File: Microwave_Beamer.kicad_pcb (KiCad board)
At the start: 4 copper layers, 200 x 170 mm, 409 parts, among them IC1 MAX2870ETJ+, U1 SKY13575-639LF, U10 SKY13575-639LF, U11 SKY13575-639LF, U12 SKY13575-639LF, U13 SE5023L-R, U14 SE5023L-R, U15 SE5023L-R, U16 SE5023L-R, U17 SE5023L-R, U18 SE5023L-R, U19 SE5023L-R, U2 SKY13575-639LF, U20 SE5023L-R, U21 SE5023L-R, U22 SE5023L-R, U23 SE5023L-R, U24 SE5023L-R, U25 SE5023L-R, U26 SE5023L-R, U27 SE5023L-R, U28 SE5023L-R, U29 SE5023L-R, U3 SKY13575-639LF, U30 SE5023L-R, U31 SE5023L-R, U32 SE5023L-R, U33 SE5023L-R, U34 SE5023L-R, U35 SE5023L-R, U36 SE5023L-R, U37 SE5023L-R, U38 SE5023L-R, U39 SE5023L-R, U4 SKY13575-639LF, U40 SE5023L-R, U41 SE5023L-R, U42 SE5023L-R, U43 SE5023L-R, U44 SE5023L-R, U45 SE5023L-R, U46 SE5023L-R, U47 SE5023L-R, U48 SE5023L-R, U49 SE5023L-R, U5 SKY13575-639LF, U50 LDL1117S33R, U51 SN74LVC1G14DCKR, U52 MIC5219-2.85YM5-TR, U53 SN74LVC1G14DCKR, U54 74HC138D, U55 TPS548D26RXXR, U56 PI_PICO, U57 SN74LVC1G14DCKR, U6 SKY13575-639LF, U7 SKY13575-639LF, U8 SKY13575-639LF, U9 SKY13575-639LF, Y1 ECS-3225MVQ-1000-CN-TR

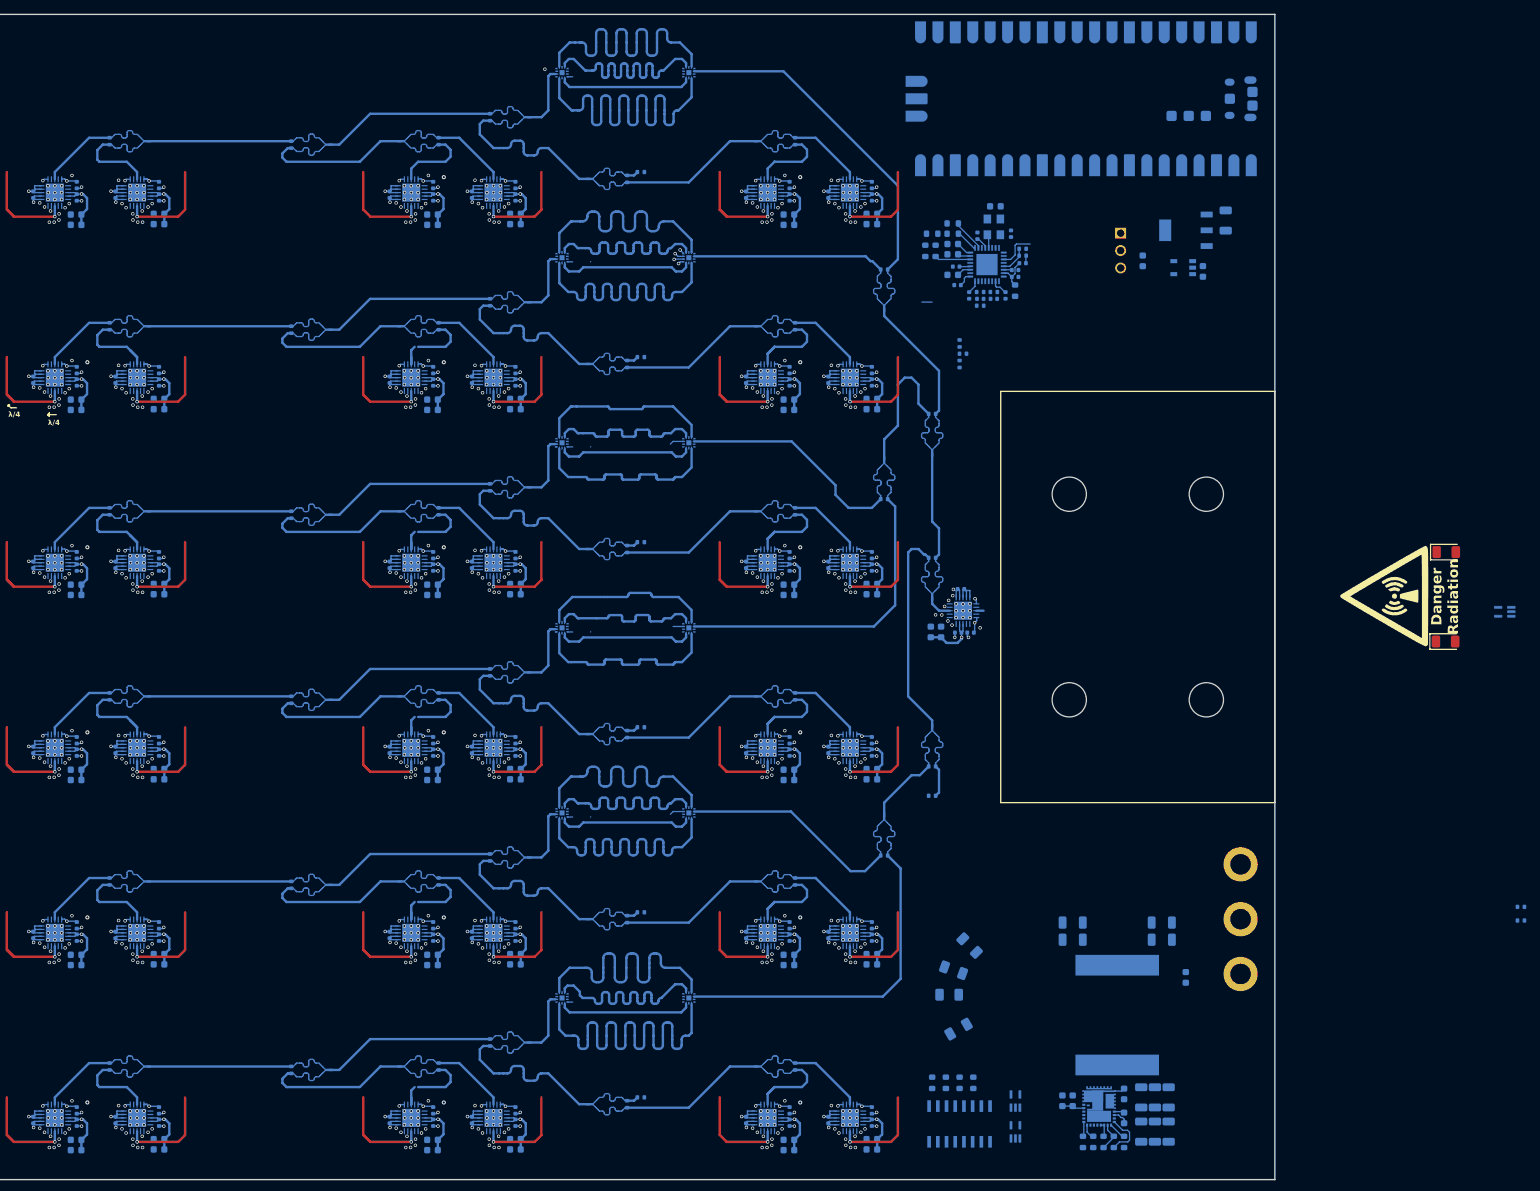
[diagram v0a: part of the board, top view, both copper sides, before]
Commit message: 6 layers now
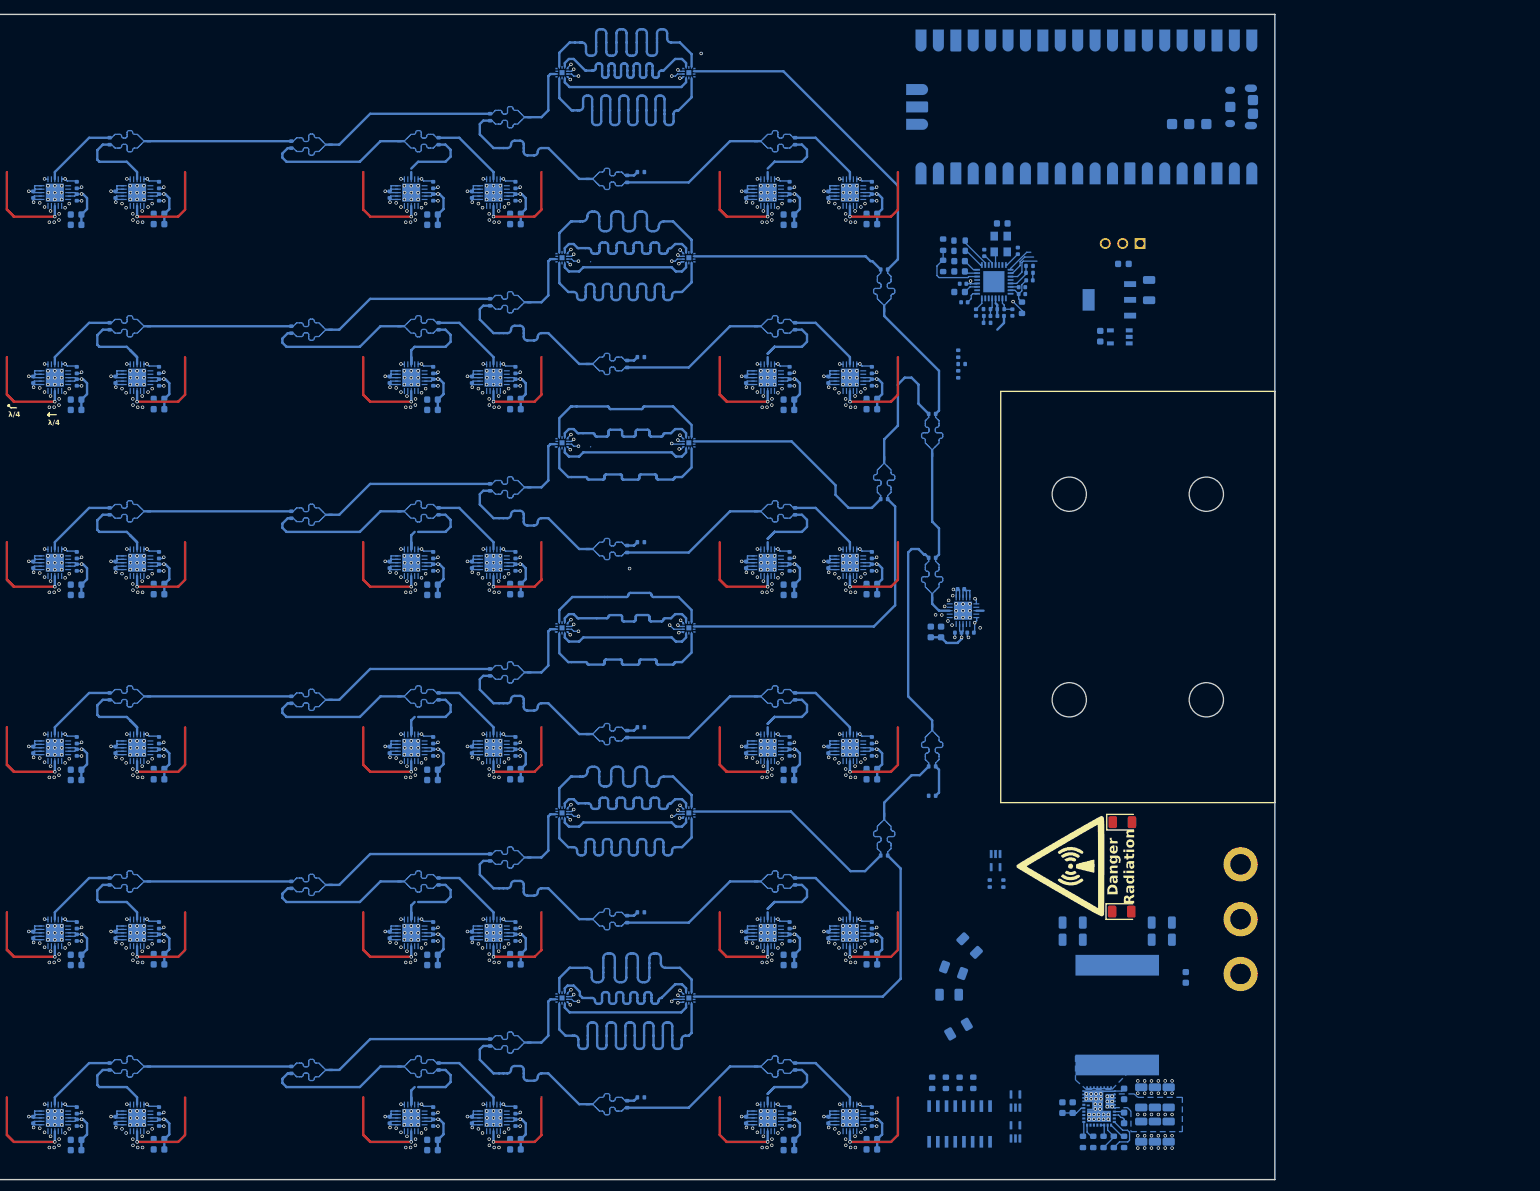
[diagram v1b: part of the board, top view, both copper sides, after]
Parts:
- removed R55: 10K, Resistor_SMD:R_0603_1608Metric
- moved U57 82.7 mm to (169.2, 128.5), turned to -90 degrees
- moved R60 77.6 mm to (168.4, 131.8), turned to -90 degrees
- moved R61 75.7 mm to (170.4, 131.8), turned to -90 degrees
- moved D5 61.5 mm to (187.7, 135.9)
- moved G*** 61.5 mm to (178.7, 129.3)
- moved D6 61.5 mm to (187.8, 122.8)
- moved C284 17.7 mm to (184.5, 52.0)
- moved U50 15.1 mm to (185.8, 46.6)
- moved CB13 15.1 mm to (191.7, 45.2)
- moved U52 13.7 mm to (187.4, 52.1)
- moved PS1 3.49 mm to (187.8, 36.6), turned to 180 degrees
- moved R48 3.41 mm to (161.6, 41.7), turned to 90 degrees
- moved C283 2.86 mm to (187.9, 41.4), turned to 0 degrees
- moved C1 2.69 mm to (168.0, 49.0)
- moved C135 2.69 mm to (164.0, 42.5)
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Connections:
- ? pad : (no net) -> +5V
- ? pad : (no net) -> +12V
- ? pad : (no net) -> GND
- C102 pad 1: /STEM/FAN_F/POWER AMP3/VCC -> +5V
- C103 pad 1: /STEM/FAN_C/POWER AMP3/VCC -> +5V
- C145 pad 1: /STEM/FAN_D/POWER AMP3/VCC -> +5V
- C187 pad 1: /STEM/FAN_E/POWER AMP3/VCC -> +5V
- C229 pad 1: /STEM/FAN_F/POWER AMP3/VCC -> +5V
- C26 pad 1: /STEM/FAN_A/POWER AMP3/VCC -> +5V
- C28 pad 1: /STEM/FAN_C/POWER AMP3/VCC -> +5V
- C286 pad 1: /STEM/FAN_A/POWER AMP3/VCC -> +5V
- C289 pad 1: /STEM/FAN_B/POWER AMP3/VCC -> +5V
- C292 pad 1: /STEM/FAN_C/POWER AMP3/VCC -> +5V
- C295 pad 1: /STEM/FAN_D/POWER AMP3/VCC -> +5V
- C298 pad 1: /STEM/FAN_E/POWER AMP3/VCC -> +5V
- C301 pad 1: /STEM/FAN_F/POWER AMP3/VCC -> +5V
- C39 pad 1: /STEM/FAN_D/POWER AMP3/VCC -> +5V
- C43 pad 1: /STEM/FAN_E/POWER AMP3/VCC -> +5V
- C48 pad 1: /STEM/FAN_F/POWER AMP3/VCC -> +5V
- C6 pad 1: /STEM/FAN_A/POWER AMP3/VCC -> +5V
- C60 pad 1: /STEM/FAN_A/POWER AMP3/VCC -> +5V
- C61 pad 1: /STEM/FAN_B/POWER AMP3/VCC -> +5V
- C64 pad 1: /STEM/FAN_B/POWER AMP3/VCC -> +5V
- C76 pad 1: /STEM/FAN_C/POWER AMP3/VCC -> +5V
- C79 pad 1: /STEM/FAN_D/POWER AMP3/VCC -> +5V
- C9 pad 1: /STEM/FAN_B/POWER AMP3/VCC -> +5V
- C91 pad 1: /STEM/FAN_E/POWER AMP3/VCC -> +5V
- IC1 pad 2: /MOSI -> MOSI
- IC1 pad 25: Net-(IC1-LD) -> unconnected-(IC1-LD-Pad25)
- IC1 pad 26: /RF_EN -> RF_EN
- IC1 pad 3: /LE -> LE
- IC1 pad 30: unconnected-(IC1-MUX_OUT-Pad30) -> MISO/SDO
- IC1 pad 4: /Chip_EN -> CHIP_EN
- R49 pad 2: unconnected-(R49-Pad2) -> GND
- R53 pad 2: /RF_EN -> RF_EN
- R54 pad 1: Net-(R54-Pad1) -> +3.3V
- R54 pad 2: Net-(IC1-LD) -> CHIP_EN
- U16 pad 18: /STEM/FAN_A/POWER AMP3/VCC -> +5V
- U16 pad 19: /STEM/FAN_A/POWER AMP3/VCC -> +5V
- U16 pad 20: /STEM/FAN_A/POWER AMP3/VCC -> +5V
- U16 pad 8: /STEM/FAN_A/POWER AMP3/VCC -> +5V
- U16 pad 9: /STEM/FAN_A/POWER AMP3/VCC -> +5V
- U21 pad 18: /STEM/FAN_B/POWER AMP3/VCC -> +5V
- U21 pad 19: /STEM/FAN_B/POWER AMP3/VCC -> +5V
- U21 pad 20: /STEM/FAN_B/POWER AMP3/VCC -> +5V
- U21 pad 8: /STEM/FAN_B/POWER AMP3/VCC -> +5V
- U21 pad 9: /STEM/FAN_B/POWER AMP3/VCC -> +5V
- U27 pad 18: /STEM/FAN_C/POWER AMP3/VCC -> +5V
- U27 pad 19: /STEM/FAN_C/POWER AMP3/VCC -> +5V
- U27 pad 20: /STEM/FAN_C/POWER AMP3/VCC -> +5V
- U27 pad 8: /STEM/FAN_C/POWER AMP3/VCC -> +5V
- U27 pad 9: /STEM/FAN_C/POWER AMP3/VCC -> +5V
- U33 pad 18: /STEM/FAN_D/POWER AMP3/VCC -> +5V
- U33 pad 19: /STEM/FAN_D/POWER AMP3/VCC -> +5V
- U33 pad 20: /STEM/FAN_D/POWER AMP3/VCC -> +5V
- U33 pad 8: /STEM/FAN_D/POWER AMP3/VCC -> +5V
- U33 pad 9: /STEM/FAN_D/POWER AMP3/VCC -> +5V
- U39 pad 18: /STEM/FAN_E/POWER AMP3/VCC -> +5V
- U39 pad 19: /STEM/FAN_E/POWER AMP3/VCC -> +5V
- U39 pad 20: /STEM/FAN_E/POWER AMP3/VCC -> +5V
- U39 pad 8: /STEM/FAN_E/POWER AMP3/VCC -> +5V
- U39 pad 9: /STEM/FAN_E/POWER AMP3/VCC -> +5V
- U45 pad 18: /STEM/FAN_F/POWER AMP3/VCC -> +5V
- U45 pad 19: /STEM/FAN_F/POWER AMP3/VCC -> +5V
- U45 pad 20: /STEM/FAN_F/POWER AMP3/VCC -> +5V
- U45 pad 8: /STEM/FAN_F/POWER AMP3/VCC -> +5V
- U45 pad 9: /STEM/FAN_F/POWER AMP3/VCC -> +5V
- U52 pad 3: /AMP_enable -> RF_EN
- U56 pad 10: unconnected-(U56-GP7-Pad10) -> RF_EN
- U56 pad 15: unconnected-(U56-GP11-Pad15) -> PHASE_CTRL_2
- U56 pad 16: unconnected-(U56-GP12-Pad16) -> PHASE_CTRL_1
- U56 pad 4: unconnected-(U56-GP2-Pad4) -> CLK
- U56 pad 5: unconnected-(U56-GP3-Pad5) -> MOSI
- U56 pad 6: unconnected-(U56-GP4-Pad6) -> MISO/SDO
- U56 pad 7: unconnected-(U56-GP5-Pad7) -> LE
- U56 pad 9: unconnected-(U56-GP6-Pad9) -> CHIP_EN
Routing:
- net 2.85VREF: track 319.1 -> 952.1 mm
- net +3.3V: track 16.8 -> 301.7 mm, vias 1 -> 13
- net +5V: track 679.8 -> 521.6 mm, vias 61 -> 73
- net ~{PHASE_CTRL_2}: track 0.00 -> 152.3 mm, vias 0 -> 6
- net PHASE_CTRL_2: track 1.40 -> 150.7 mm, vias 1 -> 7
- net ~{PHASE_CTRL_1}: track 0.00 -> 146.3 mm, vias 0 -> 6
- net PHASE_CTRL_1: track 0.80 -> 146.5 mm, vias 1 -> 6
- net /STEM/FAN_A/POWER AMP3/VCC: track 22.0 -> 0.00 mm, vias 2 -> 0
- net /STEM/FAN_F/POWER AMP3/VCC: track 22.0 -> 0.00 mm, vias 2 -> 0
- net /STEM/FAN_E/POWER AMP3/VCC: track 22.0 -> 0.00 mm, vias 2 -> 0
- net /STEM/FAN_D/POWER AMP3/VCC: track 22.0 -> 0.00 mm, vias 2 -> 0
- net /STEM/FAN_C/POWER AMP3/VCC: track 22.0 -> 0.00 mm, vias 2 -> 0
- net /STEM/FAN_B/POWER AMP3/VCC: track 22.0 -> 0.00 mm, vias 2 -> 0
- net Net-(IC1-TUNE): track 1.61 -> 11.4 mm, vias 0 -> 2
- net LE: track 0.00 -> 5.62 mm
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- added copper zone on B.Cu, net +12V
- added copper zone on In1.Cu, net GND
- added copper zone on In4.Cu, net GND
- added copper zone on B.Cu, net Net-(L4-Pad1)
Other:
- copper layers 4 -> 6
